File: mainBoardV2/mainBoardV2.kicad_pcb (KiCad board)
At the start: 2 copper layers, 55.9 x 117 mm, 33 parts, among them J1 USB4125-GF-A_REVA2, U2 ESP32-DEVKITC-32E, U3 MCP73871-2AAI_ML, U4 MPU6050_Module, U5 TPS61090RSARG4

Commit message: 3.2.26.C2
Q&A with Ricardo
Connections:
- L1 pad 1: Net-(U3-VBAT_SENSE) -> /SW
- L1 pad 2: Net-(L1-Pad2) -> Net-(U3-VBAT_SENSE)
- U5 pad 3: Net-(L1-Pad2) -> /SW
- U5 pad 4: Net-(L1-Pad2) -> /SW
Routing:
- added copper zone on F.Cu, net /SW
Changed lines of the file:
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@@
 	(net 7 "Net-(J1-CC1)")
 	(net 8 "unconnected-(J1-SHIELD-PadS1)_3")
-	(net 9 "Net-(U1-5V)")
-	(net 10 "Net-(U1-GPIO0)")
+	(net 9 "/SW")
+	(net 10 "Net-(RintoCam1-Pad1)")
 	(net 11 "unconnected-(U2-IO12-PadJ2_13)")
 	(net 12 "unconnected-(U2-IO26-PadJ2_10)")
@@
 	(net 50 "Net-(U3-STAT1{slash}*LBO)")
 	(net 51 "Net-(U3-~{PG})")
-	(net 52 "Net-(L1-Pad2)")
+	(net 52 "Net-(U2-IO32)")
 	(net 53 "Net-(U5-LBI)")
 	(net 54 "unconnected-(U5-VOUT-Pad16)")
@@
 			(layers "F.Cu" "F.Mask" "F.Paste")
 			(roundrect_rratio 0.15)
-			(net 52 "Net-(L1-Pad2)")
+			(net 9 "/SW")
 			(pinfunction "SW")
 			(pintype "input")
@@
 			(layers "F.Cu" "F.Mask" "F.Paste")
 			(roundrect_rratio 0.15)
-			(net 52 "Net-(L1-Pad2)")
+			(net 9 "/SW")
 			(pinfunction "SW")
 			(pintype "input")
@@
 			(layers "*.Cu" "*.Mask")
 			(remove_unused_layers no)
-			(net 10 "Net-(U1-GPIO0)")
+			(net 52 "Net-(U2-IO32)")
 			(pinfunction "IO32")
 			(pintype "bidirectional")
@@
 			(layers "F.Cu" "F.Mask" "F.Paste")
 			(roundrect_rratio 0.15)
-			(net 40 "Net-(U3-VBAT_SENSE)")
+			(net 9 "/SW")
 			(pinfunction "1")
 			(pintype "passive")
@@
 			(layers "F.Cu" "F.Mask" "F.Paste")
 			(roundrect_rratio 0.15)
-			(net 52 "Net-(L1-Pad2)")
+			(net 40 "Net-(U3-VBAT_SENSE)")
 			(pinfunction "2")
 			(pintype "passive")
@@
 			(layers "F.Cu" "F.Mask" "F.Paste")
 			(roundrect_rratio 0.208333)
-			(net 9 "Net-(U1-5V)")
+			(net 10 "Net-(RintoCam1-Pad1)")
 			(pintype "passive")
 		)
@@
 	)
 	(segment
+		(start 102.004 104.956)
+		(end 102.004 104.996)
+		(width 0.2)
+		(layer "B.Cu")
+		(net 4)
+	)
+	(segment
 		(start 94.946 121.666)
 		(end 98.956 117.656)
@@
 	)
 	(segment
+		(start 102.004 104.996)
+		(end 102 105)
+		(width 0.2)
+		(layer "B.Cu")
+		(net 4)
+	)
+	(segment
 		(start 93.726 75.184)
 		(end 104.394 85.852)
@@
 		(width 0.2)
 		(layer "F.Cu")
-		(net 9)
+		(net 10)
 	)
 	(segment
@@
 	)
 	(zone
-		(net 2)
-		(net_name "+5V")
+		(net 9)
+		(net_name "/SW")
 		(layer "F.Cu")
 		(name "-VBatt")

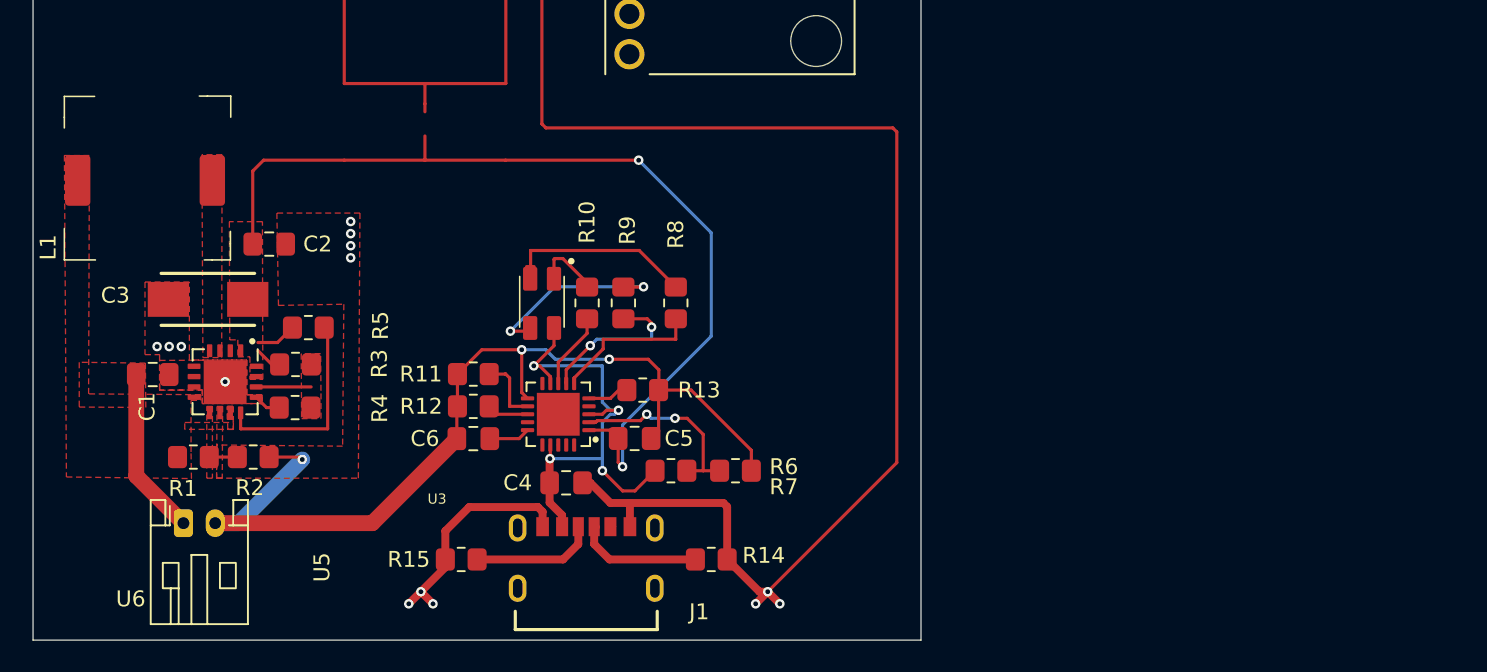
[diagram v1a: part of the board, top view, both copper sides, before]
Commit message: 3.7.26.C1
removed the old boost converter chip and circuit and put in the new one. Unconnected.
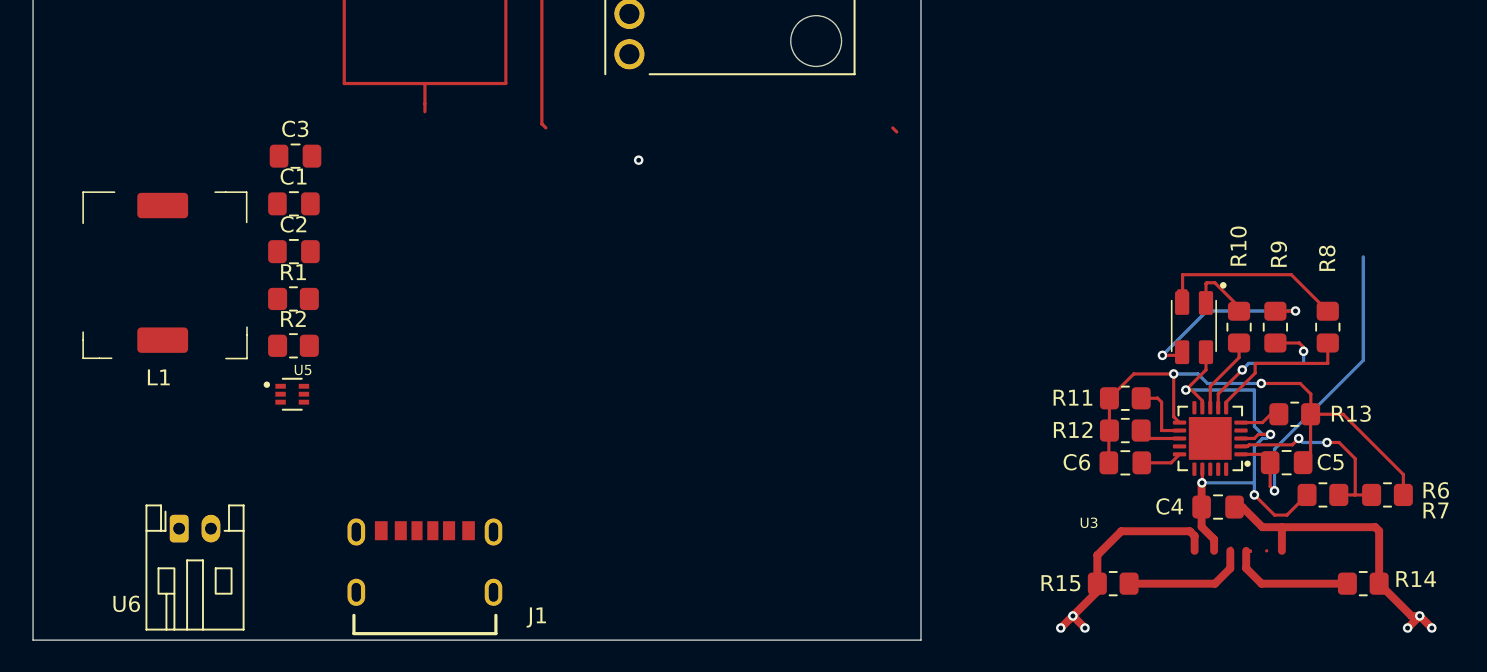
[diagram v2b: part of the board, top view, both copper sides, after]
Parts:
- removed R3: 1.07M, Resistor_SMD:R_0805_2012Metric_Pad1.20x1.40mm_HandSolder
- removed R4: 200k, Resistor_SMD:R_0805_2012Metric_Pad1.20x1.40mm_HandSolder
- removed R5: 1M, Resistor_SMD:R_0805_2012Metric_Pad1.20x1.40mm_HandSolder
- C2: value 2.2uF -> 22uF
- C3: value 100uF -> 22uF; footprint T495C107K006ATE150(1):CAPMP6032X250 -> Capacitor_SMD:C_0805_2012Metric_Pad1.18x1.45mm_HandSolder
- L1: value 6.8uH -> 1uH
- R1: value 390k -> 766k
- R2: value 500k -> 100k
- U5: value TPS61090RSARG4 -> TPS61023DRLT; footprint TPS61090RSARG4:QFN65P400X400X100-17N -> TPS61023DRLT:SOT50P160X60-6N
- moved C6 41.1 mm to (150.8, 117.9)
- moved R10 41.1 mm to (158.0, 109.3)
- moved R11 41.1 mm to (150.8, 113.8)
- moved R12 41.1 mm to (150.8, 115.8)
- moved R13 41.1 mm to (161.5, 114.8)
- moved R15 41.1 mm to (150.0, 125.5)
- moved R9 41.1 mm to (160.2, 109.3)
- moved C4 41.1 mm to (156.6, 120.7)
- moved C5 41.1 mm to (160.9, 117.9)
- moved R14 41.1 mm to (165.8, 125.5)
- moved R6 41.1 mm to (163.2, 119.9)
- moved R7 41.1 mm to (167.3, 119.9)
- moved R8 41.1 mm to (163.5, 109.3)
- moved U3 41.1 mm to (156.1, 116.3)
- moved U7 41.1 mm to (154.4, 107.8)
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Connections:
- C1 pad 1: Net-(U3-VBAT_SENSE) -> /VBatt+
- C2 pad 1: Net-(SW1-A) -> /VoutBoost
- C4 pad 1: +5V -> Net-(U3-CE)
- C5 pad 1: Net-(SW1-A) -> Net-(C5-Pad1)
- L1 pad 2: Net-(U3-VBAT_SENSE) -> /VBatt+
- R1 pad 1: Net-(U3-VBAT_SENSE) -> /VoutBoost
- R1 pad 2: Net-(U5-LBI) -> /Boost FB
- R2 pad 2: Net-(U5-LBI) -> /Boost FB
- R6 pad 1: +5V -> Net-(U3-CE)
- U3 pad 1: Net-(SW1-A) -> Net-(C5-Pad1)
- U3 pad 17: +5V -> Net-(U3-CE)
- U3 pad 18: +5V -> Net-(U3-CE)
- U3 pad 19: +5V -> Net-(U3-CE)
- U3 pad 20: Net-(SW1-A) -> Net-(C5-Pad1)
- U3 pad 3: +5V -> Net-(U3-CE)
- U3 pad 4: +5V -> Net-(U3-CE)
- U3 pad 9: +5V -> Net-(U3-CE)
- U5 pad 1: Net-(SW1-A) -> /Boost FB
- U5 pad 2: (no net) -> /VBatt+
- U5 pad 3: /SW -> /VBatt+
- U5 pad 4: /SW -> GND
- U5 pad 5: GND -> /SW
- U5 pad 6: GND -> /VoutBoost
- U6 pad 1: Net-(U3-VBAT_SENSE) -> unconnected-(U6-VBAT+-Pad1)
- U6 pad 2: GND -> unconnected-(U6-VBAT--Pad2)
- U7 pad 4: +5V -> Net-(U3-CE)
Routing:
- net GND: track 216.9 -> 121.2 mm, vias 19 -> 10
- net Net-(SW1-A): track 129.0 -> 66.5 mm, vias 2 -> 0
- net +5V: track 32.0 -> 0.01 mm, vias 4 -> 0
- net Net-(U3-CE): track 0.00 -> 32.0 mm, vias 0 -> 4
- net Net-(C5-Pad1): track 0.00 -> 21.0 mm, vias 0 -> 2
- net Net-(U3-VBAT_SENSE): track 12.7 -> 2.06 mm
- net Net-(U5-FB): track 3.46 -> 0.00 mm
- net Net-(U5-LBI): track 1.77 -> 0.00 mm
- removed copper zone on F.Cu, net (none)
- removed copper zone on F.Cu, net +5V
- removed copper zone on F.Cu, net /SW
- removed copper zone on F.Cu, net Net-(SW1-A)

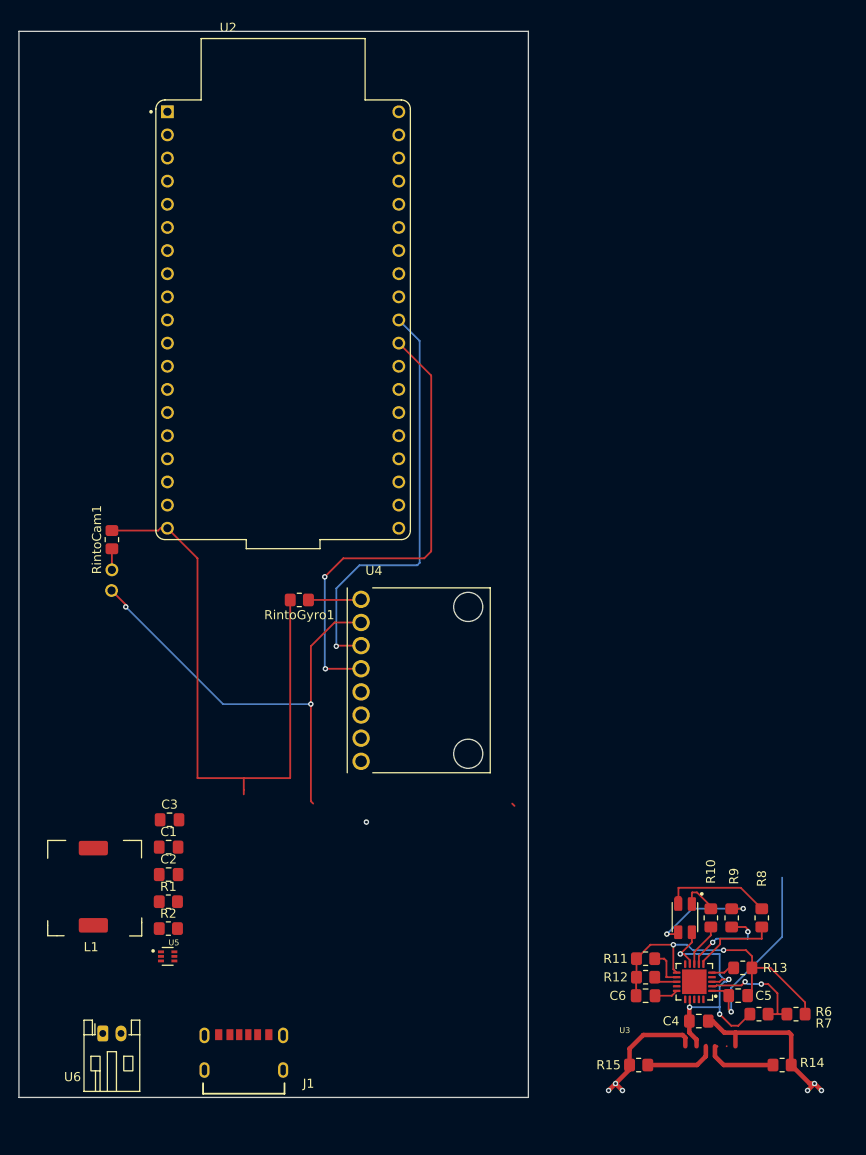
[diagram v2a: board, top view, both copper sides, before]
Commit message: 3.9.26.Cf
Closing the 3.9 session as it ran into 3.10. boost circuit ready to be optimally connected.

Charger ready for a fresh start.

Warning about 3 unconnected vias currently. Don't see them yet.
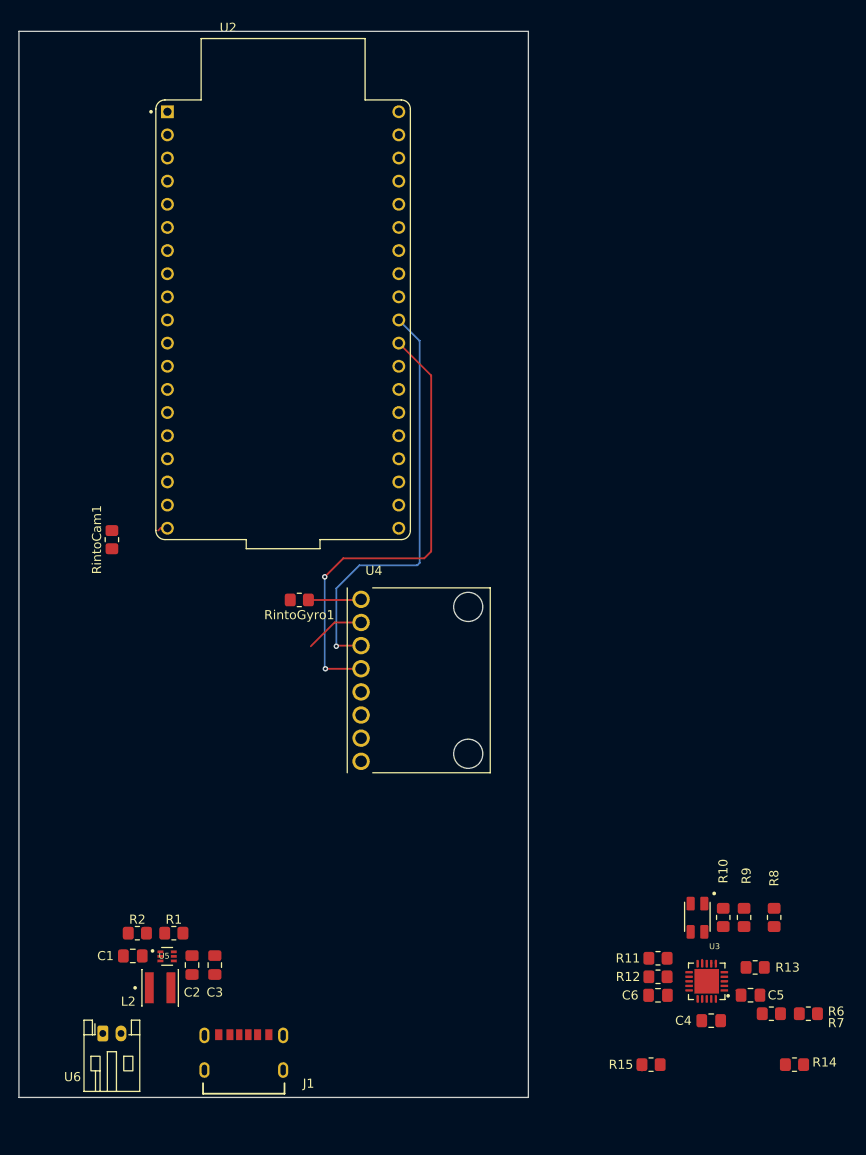
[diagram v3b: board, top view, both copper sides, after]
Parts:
- removed ? (x2): , 
- removed L1: 1uH, Inductor_SMD:Sumida_senior
- added L2: XEL4030-102MEC, XEL4030-102MEC:IND_XEL4030-102MEC, F.Cu at (97.5, 117.0)
- moved C3 16.7 mm to (103.5, 114.5), turned to -90 degrees
- moved C1 12.6 mm to (94.5, 113.5), turned to 180 degrees
- moved C2 10.3 mm to (101.0, 114.5), turned to -90 degrees
- moved R1 3.51 mm to (99.0, 111.0), turned to 180 degrees
- moved R2 3.44 mm to (95.0, 111.0)
- moved C4 1.36 mm to (158.0, 120.6)
- moved C6 1.36 mm to (152.2, 117.8)
- moved R10 1.36 mm to (159.3, 109.3)
- moved R11 1.36 mm to (152.2, 113.8)
- moved R12 1.36 mm to (152.2, 115.8)
- moved R13 1.36 mm to (162.8, 114.8)
- moved R6 1.36 mm to (164.6, 119.8)
- moved R7 1.36 mm to (168.7, 119.8)
- moved R8 1.36 mm to (164.9, 109.3)
- moved R9 1.36 mm to (161.6, 109.3)
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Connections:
- net Net-(C5-Pad1) renamed /VoutCharger
- net Net-(U3-CE) renamed /5VUSB
- net Net-(U3-PROG1) renamed /PROG1
- net Net-(U3-PROG3) renamed /PROG3
- net Net-(U3-VPCC) renamed /VPCC
- C6 pad 1: Net-(U3-VBAT_SENSE) -> /VBatt+
- R10 pad 1: Net-(U7-Red) -> /LowBatt
- R10 pad 2: Net-(U3-STAT1/*LBO) -> Net-(U7-Red)
- R13 pad 1: Net-(U3-THERM) -> GND
- R13 pad 2: GND -> /Therm
- R9 pad 1: Net-(U7-Yellow) -> /ChargeDone
- R9 pad 2: Net-(U3-STAT2) -> Net-(U7-Green)
- RintoCam1 pad 1: Net-(RintoCam1-Pad1) -> unconnected-(RintoCam1-Pad1)
- RintoCam1 pad 2: Net-(SW1-A) -> unconnected-(RintoCam1-Pad2)
- RintoGyro1 pad 1: Net-(RintoGyro1-Pad1) -> unconnected-(RintoGyro1-Pad1)
- RintoGyro1 pad 2: Net-(SW1-A) -> unconnected-(RintoGyro1-Pad2)
- U2 pad J2_19: Net-(SW1-A) -> unconnected-(U2-EXT_5V-PadJ2_19)
- U2 pad J2_7: Net-(U2-IO32) -> unconnected-(U2-IO32-PadJ2_7)
- U2 pad J3_10: Net-(U2-IO5) -> unconnected-(U2-IO5-PadJ3_10)
- U2 pad J3_11: Net-(U2-IO17) -> unconnected-(U2-IO17-PadJ3_11)
- U3 pad 14: Net-(U3-VBAT_SENSE) -> /VBatt+
- U3 pad 15: Net-(U3-VBAT_SENSE) -> /VBatt+
- U3 pad 16: Net-(U3-VBAT_SENSE) -> /VBatt+
- U3 pad 5: Net-(U3-THERM) -> /Therm
- U3 pad 6: Net-(U3-~{PG}) -> unconnected-(U3-~{PG}-Pad6)
- U3 pad 7: Net-(U3-STAT2) -> /ChargeDone
- U3 pad 8: Net-(U3-STAT1/*LBO) -> /LowBatt
- U4 pad GND: GND -> unconnected-(U4-PadGND)
- U4 pad SCL: Net-(U2-IO5) -> unconnected-(U4-PadSCL)
- U4 pad SDA: Net-(U2-IO17) -> unconnected-(U4-PadSDA)
- U4 pad VCC: Net-(RintoGyro1-Pad1) -> unconnected-(U4-PadVCC)
- U6 pad 1: unconnected-(U6-VBAT+-Pad1) -> /VBatt+
- U6 pad 2: unconnected-(U6-VBAT--Pad2) -> GND
- U7 pad 2: Net-(U7-Yellow) -> unconnected-(U7-Yellow-Pad2)
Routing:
- net GND: track 121.2 -> 1.74 mm, vias 10 -> 0
- net (no net): track 0.00 -> 104.1 mm, vias 0 -> 3
- net Net-(SW1-A): track 66.5 -> 0.00 mm
- net Net-(U2-IO17): track 51.3 -> 0.00 mm, vias 2 -> 0
- net Net-(U2-IO5): track 47.0 -> 0.00 mm, vias 1 -> 0
- net /5VUSB: track 32.0 -> 0.45 mm, vias 4 -> 0
- net /VoutCharger: track 21.0 -> 0.76 mm, vias 2 -> 0
- net Net-(U7-Green): track 12.4 -> 0.05 mm
- net /VPCC: track 12.3 -> 0.00 mm, vias 2 -> 0
- net Net-(U7-Yellow): track 12.1 -> 0.00 mm, vias 2 -> 0
- net Net-(U3-STAT2): track 10.0 -> 0.00 mm, vias 2 -> 0
- net Net-(U3-~{PG}): track 9.41 -> 0.00 mm
- net Net-(J1-CC1): track 8.05 -> 0.00 mm
- net Net-(J1-CC2): track 7.91 -> 0.00 mm
- net unconnected-(U4-PadGND): track 0.00 -> 6.59 mm
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
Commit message: 3.11.26.C1
False Start
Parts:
- moved L2 0.50 mm to (97.0, 117.0)
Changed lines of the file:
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@@
 	(footprint "XEL4030-102MEC:IND_XEL4030-102MEC"
 		(layer "F.Cu")
-		(at 97.5 117)
+		(at 97 117)
 		(property "Reference" "L2"
 			(at -3.5 1.5 0)

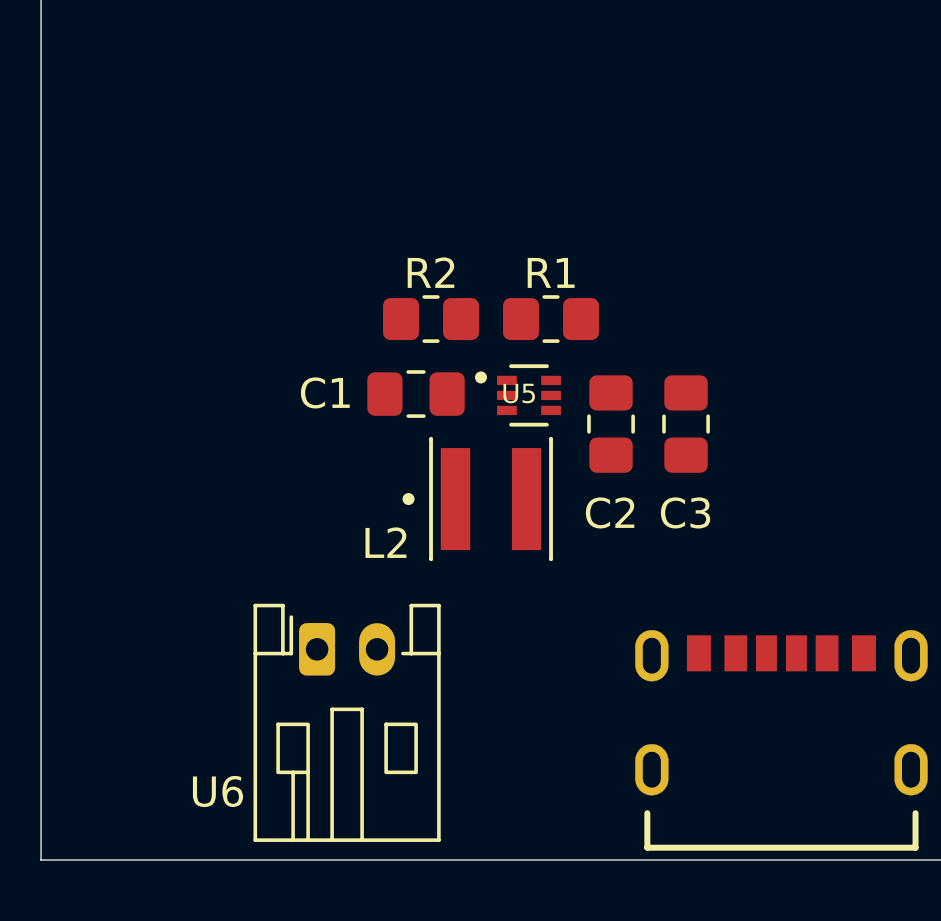
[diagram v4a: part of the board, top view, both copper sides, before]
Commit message: 3.11.26.C2
Connected nets on booster. Still need to create ground vias
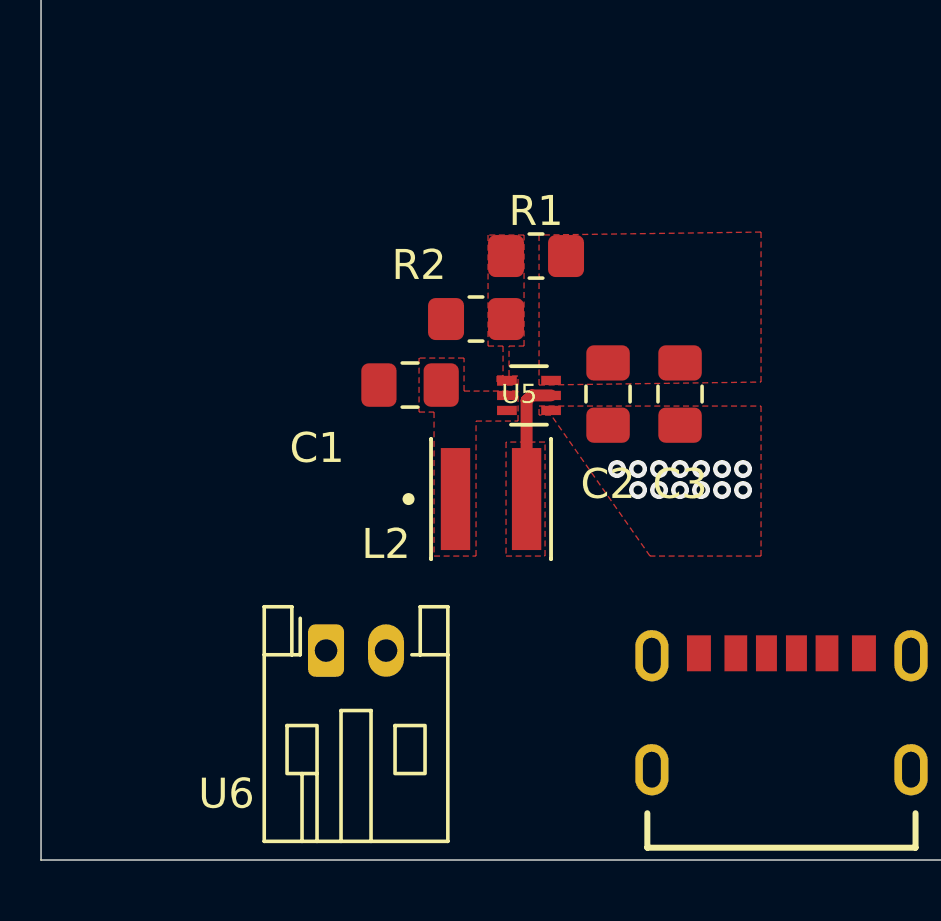
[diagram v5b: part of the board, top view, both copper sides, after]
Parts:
- moved R1 2.16 mm to (98.5, 108.9)
- moved R2 1.50 mm to (96.5, 111.0)
- moved C3 1.02 mm to (103.3, 113.5)
- moved C2 1.00 mm to (100.9, 113.5)
- moved C1 0.36 mm to (94.3, 113.2)
- moved U6 0.30 mm to (91.5, 122.0)
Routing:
- net /SW: track 0.00 -> 4.17 mm
- net GND: vias 0 -> 13
- added copper zone on F.Cu, net /Boost FB
- added copper zone on F.Cu, net /SW
- added copper zone on F.Cu, net /VBatt+
- added copper zone on F.Cu, net /VoutBoost
- added copper zone on F.Cu, net GND
